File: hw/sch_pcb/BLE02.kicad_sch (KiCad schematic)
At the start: 30 parts, among them J1 Conn_Coaxial, M1 HOLE, M2 HOLE, M3 HOLE, M4 HOLE, U2 CC2564CRVMR, X1 ASH7K-32.768KHZ-T, Y3 ECS-260-8-36CKM-TR

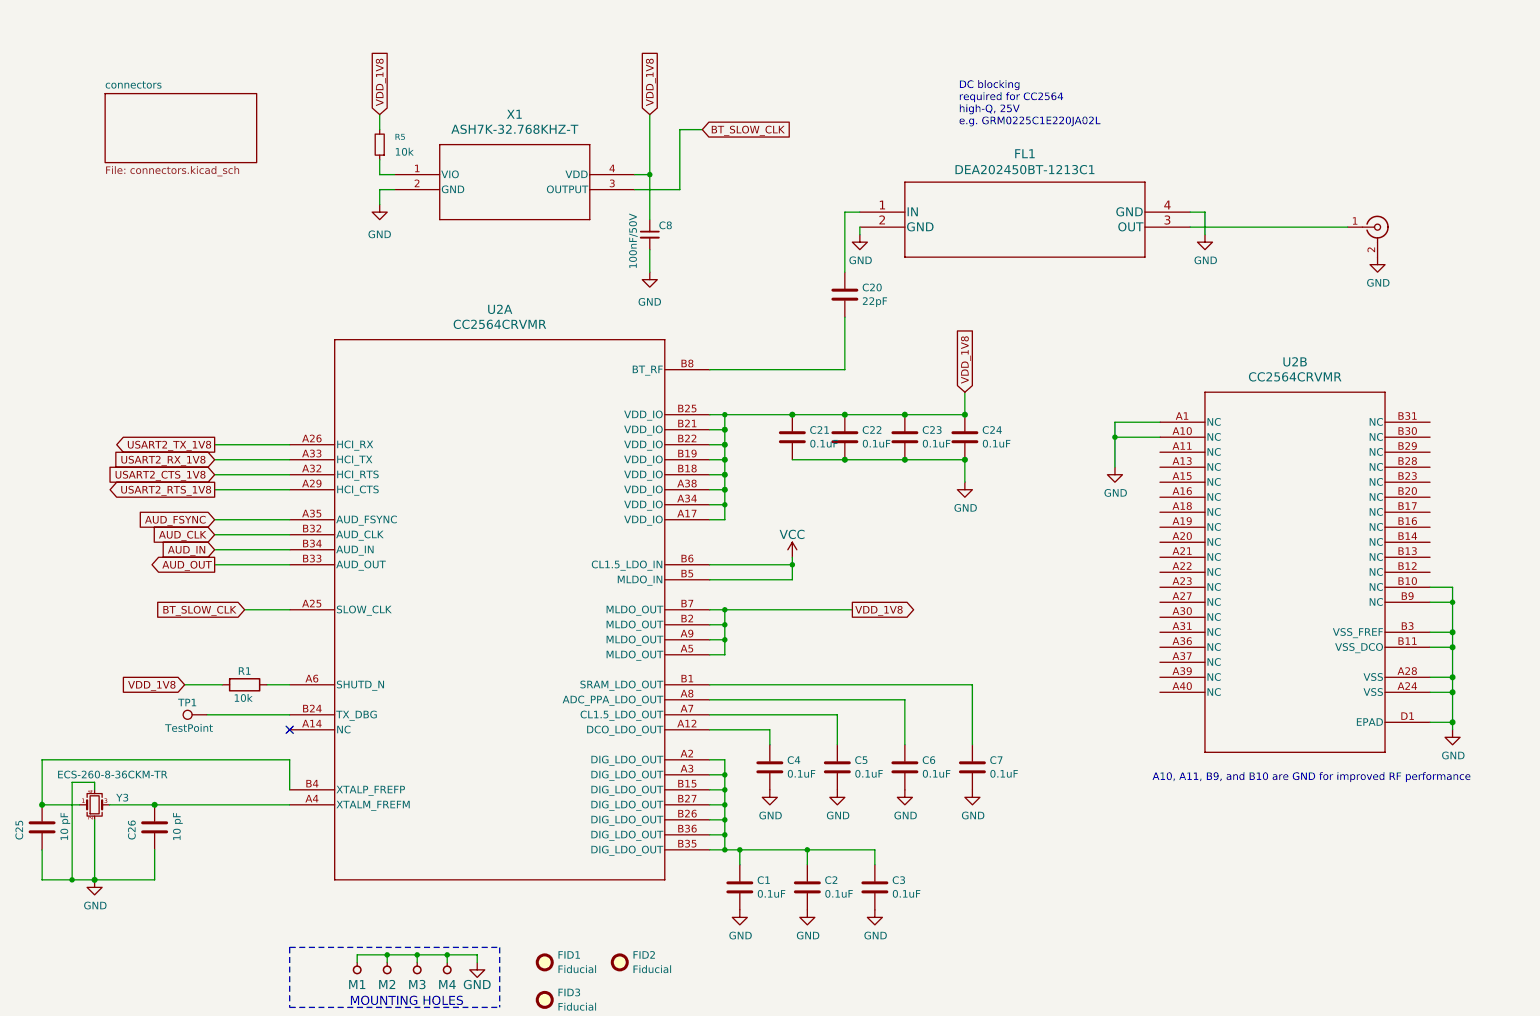
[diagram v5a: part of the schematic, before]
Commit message: Cleanup layout. Fix obsolete part types.
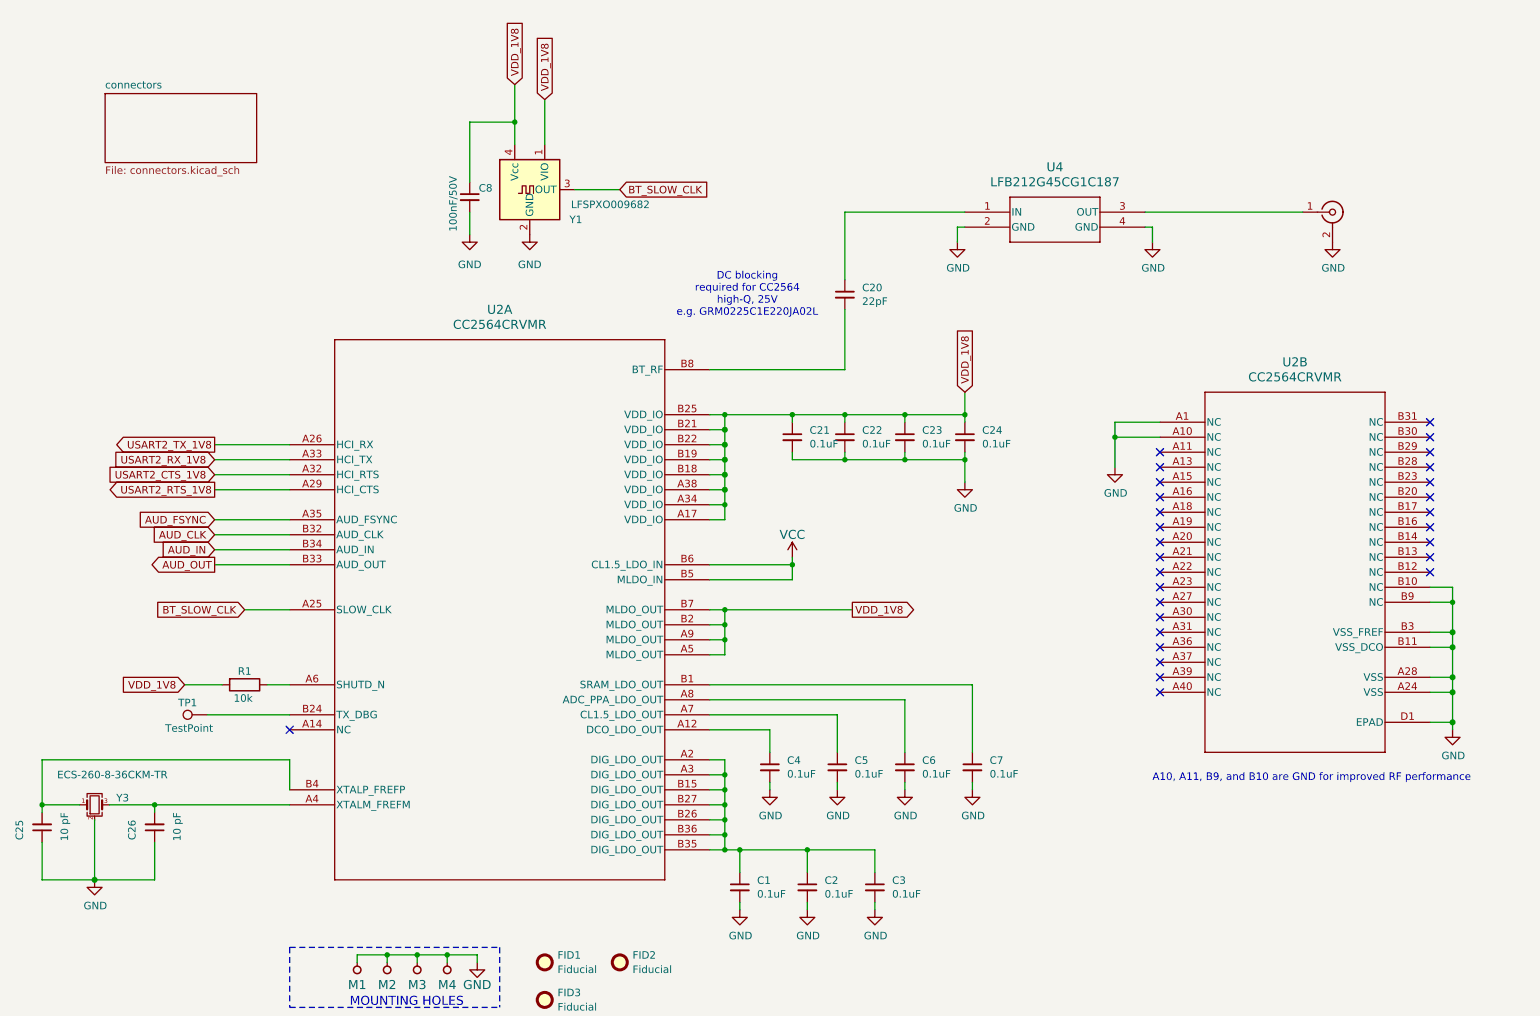
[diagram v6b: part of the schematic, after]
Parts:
- removed FL1: DEA202450BT-1213C1, cc2654-board-footprints:DEA202450BT-1213C1, symbol DEA202450BT-1213C1:DEA202450BT-1213C1
- removed R5: 10k, Resistor_SMD:R_0603_1608Metric_Pad0.98x0.95mm_HandSolder, symbol Device:R_Small
- removed X1: ASH7K-32.768KHZ-T, ASH7K_ABR, symbol MLAB_Lib:ASH7K-32.768KHZ-T
- added U4: LFB212G45CG1C187, MLAB_SAW:Murata_C187, symbol MLAB_Lib:LFB212G45CG1C187
- added Y1: LFSPXO009682, Oscillator:Oscillator_SMD_SeikoEpson_SG210-4Pin_2.5x2.0mm, symbol Oscillator:SG-3030CM
- C1, C2, C20, C21, C22, C23, C24, C25, C26, C3, C4, C5, C6, C7: symbol cc2564-board-rescue:C-Device -> Device:C_Small
- C8: footprint Capacitor_SMD:C_0603_1608Metric_Pad1.08x0.95mm_HandSolder -> Capacitor_SMD:C_0603_1608Metric
- U2: footprint MLAB_Lib:RVM0076A -> Mlab_IO:RVM0076A
- U2: footprint RVM0076A -> Mlab_IO:RVM0076A
- Y3: footprint cc2654-board-footprints:XTAL_ECS-260-8-36CKM-TR -> Crystal:Crystal_SMD_2520-4Pin_2.5x2.0mm; symbol cc2564-board-rescue:Crystal_GND24_Small-Device -> Device:Crystal_GND24_Small; UST_ID (none) -> 64c9715d76c82a1d3b579549
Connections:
- net BT_SLOW_CLK: now also Y1.3 (OUT)
- net GND: now also U4.2 (GND), U4.4 (GND), Y1.2 (GND)
- net VDD_1V8: now also Y1.1 (VIO), Y1.4 (Vcc)
- net at C20.1: now also U4.1 (IN)
- net at J1.1 (In): now also U4.3 (OUT)
- no-connect marks 1 -> 29
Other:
- moved on the sheet: C8

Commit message: Update UST_IDs.
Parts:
- C1, C2, C21, C22, C23, C24, C3, C4, C5, C6, C7: value 0.1uF -> 100nF; UST_ID (none) -> 5c70984812875079b91f8bf2
- C20: UST_ID (none) -> 5e3ff7af1287502a33bad770
- C25, C26: UST_ID (none) -> 5c70984812875079b91f8be2
- C8: value 100nF/50V -> 100nF; UST_ID (none) -> 5c70984812875079b91f8bf2
- J1: UST_ID (none) -> 5fa10cc512875025b39779f6
- R1: UST_ID (none) -> 5c70984512875079b91f8962
- TP1: now left out of the parts list
- U2: UST_ID (none) -> 6998b45dd42e6e3c4d330db1
- U4: UST_ID (none) -> 6998b530d42e6e3c4d330dd0
- Y1: UST_ID (none) -> 6998b786d42e6e3c4d330e5b
- Y3: UST_ID 64c9715d76c82a1d3b579549 -> 6998b8c5d42e6e3c4d330e98
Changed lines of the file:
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@@
 			)
 		)
-		(property "Value" "0.1uF"
+		(property "Value" "100nF"
 			(at 156.591 93.853 0)
 			(effects
@@
 			)
 		)
+		(property "UST_ID" "5c70984812875079b91f8bf2"
+			(at 153.67 92.71 0)
+			(effects
+				(font
+					(size 1.27 1.27)
+				)
+				(hide yes)
+			)
+		)
 		(pin "1"
 		)
@@
 			)
 		)
-		(property "Value" "0.1uF"
+		(property "Value" "100nF"
 			(at 165.481 93.853 0)
 			(effects
@@
 			)
 		)
+		(property "UST_ID" "5c70984812875079b91f8bf2"
+			(at 162.56 92.71 0)
+			(effects
+				(font
+					(size 1.27 1.27)
+				)
+				(hide yes)
+			)
+		)
 		(pin "1"
 		)
@@
 			)
 		)
-		(property "Value" "0.1uF"
+		(property "Value" "100nF"
 			(at 175.641 93.853 0)
 			(effects
@@
 			)
 		)
+		(property "UST_ID" "5c70984812875079b91f8bf2"
+			(at 172.72 92.71 0)
+			(effects
+				(font
+					(size 1.27 1.27)
+				)
+				(hide yes)
+			)
+		)
 		(pin "1"
 		)
@@
 			)
 		)
-		(property "Value" "0.1uF"
+		(property "Value" "100nF"
 			(at 185.801 93.853 0)
 			(effects
@@
 			)
 		)
-		(property "UST_ID" ""
+		(property "UST_ID" "5c70984812875079b91f8bf2"
 			(at 182.88 92.71 0)
 			(effects
@@
 			)
 		)
-		(property "UST_ID" "64c9715d76c82a1d3b579549"
+		(property "UST_ID" "6998b8c5d42e6e3c4d330e98"
 			(at 35.56 154.94 0)
 			(effects
@@
 			)
 		)
+		(property "UST_ID" "5c70984812875079b91f8be2"
+			(at 26.67 158.75 90)
+			(effects
+				(font
+					(size 1.27 1.27)
+				)
+				(hide yes)
+			)
+		)
 		(pin "1"
 		)
@@
 			)
 		)
+		(property "UST_ID" "5c70984812875079b91f8be2"
+			(at 45.72 158.75 90)
+			(effects
+				(font
+					(size 1.27 1.27)
+				)
+				(hide yes)
+			)
+		)
 		(pin "1"
 		)
@@
 			)
 		)
+		(property "UST_ID" "5e3ff7af1287502a33bad770"
+			(at 162.56 68.58 0)
+			(effects
+				(font
+					(size 1.27 1.27)
+				)
+				(hide yes)
+			)
+		)
 		(pin "1"
 		)
@@
 		(unit 1)
 		(exclude_from_sim no)
-		(in_bom yes)
+		(in_bom no)
 		(on_board yes)
 		(dnp no)
@@
 			)
 		)
-		(property "UST_ID" ""
+		(property "UST_ID" "6998b530d42e6e3c4d330dd0"
 			(at 182.88 54.61 0)
 			(effects
@@
 			)
 		)
-		(property "Value" "0.1uF"
+		(property "Value" "100nF"
 			(at 187.071 149.733 0)
 			(effects
@@
 			)
 		)
+		(property "UST_ID" "5c70984812875079b91f8bf2"
+			(at 184.15 148.59 0)
+			(effects
+				(font
+					(size 1.27 1.27)
+				)
+				(hide yes)
+			)
+		)
 		(pin "1"
 		)
@@
 			)
 		)
-		(property "UST_ID" ""
+		(property "UST_ID" "6998b786d42e6e3c4d330e5b"
 			(at 109.22 50.8 0)
 			(effects
@@
 			)
 		)
-		(property "Value" "0.1uF"
+		(property "Value" "100nF"
 			(at 159.131 170.053 0)
 			(effects
@@
 			)
 		)
+		(property "UST_ID" "5c70984812875079b91f8bf2"
+			(at 156.21 168.91 0)
+			(effects
+				(font
+					(size 1.27 1.27)
+				)
+				(hide yes)
+			)
+		)
 		(pin "1"
 		)
@@
 			)
 		)
+		(property "UST_ID" "5c70984512875079b91f8962"
+			(at 60.96 134.62 90)
+			(effects
+				(font
+					(size 1.27 1.27)
+				)
+				(hide yes)
+			)
+		)
 		(pin "1"
 		)
@@
 			)
 		)
-		(property "Value" "0.1uF"
+		(property "Value" "100nF"
 			(at 170.561 170.053 0)
 			(effects
@@
 			)
 		)
+		(property "UST_ID" "5c70984812875079b91f8bf2"
+			(at 167.64 168.91 0)
+			(effects
+				(font
+					(size 1.27 1.27)
+				)
+				(hide yes)
+			)
+		)
 		(pin "1"
 		)
@@
 			)
 		)
-		(property "Value" "100nF/50V"
+		(property "Value" "100nF"
 			(at 96.266 57.912 90)
 			(effects
@@
 			)
 		)
+		(property "UST_ID" "5c70984812875079b91f8bf2"
+			(at 99.06 52.07 0)
+			(effects
+				(font
+					(size 1.27 1.27)
+				)
+				(hide yes)
+			)
+		)
 		(pin "1"
 		)
@@
 			)
 		)
-		(property "UST_ID" ""
+		(property "UST_ID" "6998b45dd42e6e3c4d330db1"
 			(at 238.76 115.57 0)
 			(effects
@@
 			)
 		)
-		(property "UST_ID" ""
+		(property "UST_ID" "6998b45dd42e6e3c4d330db1"
 			(at 104.14 121.92 0)
 			(effects
@@
 			)
 		)
-		(property "Value" "0.1uF"
+		(property "Value" "100nF"
 			(at 175.641 149.733 0)
 			(effects
@@
 			)
 		)
+		(property "UST_ID" "5c70984812875079b91f8bf2"
+			(at 172.72 148.59 0)
+			(effects
+				(font
+					(size 1.27 1.27)
+				)
+				(hide yes)
+			)
+		)
 		(pin "1"
 		)
@@
 			)
 		)
-		(property "UST_ID" ""
+		(property "UST_ID" "5fa10cc512875025b39779f6"
 			(at 245.11 54.61 0)
 			(effects
@@
 			)
 		)
-		(property "Value" "0.1uF"
+		(property "Value" "100nF"
 			(at 164.211 149.733 0)
 			(effects
@@
 			)
 		)
+		(property "UST_ID" "5c70984812875079b91f8bf2"
+			(at 161.29 148.59 0)
+			(effects
+				(font
+					(size 1.27 1.27)
+				)
+				(hide yes)
+			)
+		)
 		(pin "1"
 		)
@@
 			)
 		)
-		(property "Value" "0.1uF"
+		(property "Value" "100nF"
 			(at 147.701 170.053 0)
 			(effects
@@
 			)
 		)
+		(property "UST_ID" "5c70984812875079b91f8bf2"
+			(at 144.78 168.91 0)
+			(effects
+				(font
+					(size 1.27 1.27)
+				)
+				(hide yes)
+			)
+		)
 		(pin "1"
 		)
@@
 			)
 		)
-		(property "Value" "0.1uF"
+		(property "Value" "100nF"
 			(at 152.781 149.733 0)
 			(effects
@@
 			)
 		)
+		(property "UST_ID" "5c70984812875079b91f8bf2"
+			(at 149.86 148.59 0)
+			(effects
+				(font
+					(size 1.27 1.27)
+				)
+				(hide yes)
+			)
+		)

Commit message: Merge schematics sheet into one page.
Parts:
- added C16: 100nF, Capacitor_SMD:C_0603_1608Metric, symbol Device:C
- added C17: 10uF, Capacitor_SMD:C_0805_2012Metric, symbol Device:C
- added D1: LED, Mlab_D:LED_1206_mill, symbol Device:LED
- added D3: BZX585-B5V6.115, Diode_SMD:D_SOD-523, symbol Device:D_Zener
- added J2: 3.3V, Mlab_Pin_Headers:Straight_2x03, symbol MLAB_HEADER:HEADER_2x03_PARALLEL
- added J3, J4: JUMP_5X2, Mlab_Pin_Headers:Straight_2x04, symbol MLAB_HEADER:HEADER_2x04_PARALLEL
- added R2, R3: 10k, Resistor_SMD:R_0603_1608Metric, symbol cc2564-board-rescue:R-Device
- added R4: 2k2, Resistor_SMD:R_0603_1608Metric, symbol cc2564-board-rescue:R-Device
- added U1, U3: TXS0104EPW, Package_SO:TSSOP-14_4.4x5mm_P0.65mm, symbol Logic_LevelTranslator:TXS0104EPW
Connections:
- net AUD_CLK: now also U1.4 (A3)
- net AUD_FSYNC: now also U1.5 (A4)
- net AUD_IN: now also U1.2 (A1)
- net AUD_OUT: now also U1.3 (A2)
- net GND: now also C16.2, C17.2, D1.1 (K), D3.2 (A), J2.1, J2.2, J2.5, J2.6, U1.7 (GND), U3.7 (GND)
- net USART2_CTS_1V8: now also U3.3 (A2)
- net USART2_RTS_1V8: now also U3.5 (A4)
- net USART2_RX_1V8: now also U3.2 (A1)
- net USART2_TX_1V8: now also U3.4 (A3)
- net VCC: now also C16.1, C17.1, D3.1 (K), J2.3, J2.4, R4.1, U1.14 (V_{CCB}), U3.14 (V_{CCB})
- net VDD_1V8: now also R2.1, R3.1, U1.1 (V_{CCA}), U3.1 (V_{CCA})
- new net: J3.1, J3.2, U3.10 (B4)
- new net: J3.3, J3.4, U3.11 (B3)
- new net: J3.5, J3.6, U3.12 (B2)
- new net: J3.7, J3.8, U3.13 (B1)
- new net: D1.2 (A), R4.2
- new net: J4.1, J4.2, U1.10 (B4)
- new net: J4.3, J4.4, U1.11 (B3)
- new net: J4.5, J4.6, U1.12 (B2)
- new net: J4.7, J4.8, U1.13 (B1)
- new net: R3.2, U3.8 (OE)
- new net: R2.2, U1.8 (OE)
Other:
- removed sheet connectors
- note added: "POWER INPUT"
- moved on the sheet: C1, C2, C20, C21, C22, C23, C24, C25, C26, C3, C4, C5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
